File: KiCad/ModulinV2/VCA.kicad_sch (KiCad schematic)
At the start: 9 parts, among them IC9 AS3360D

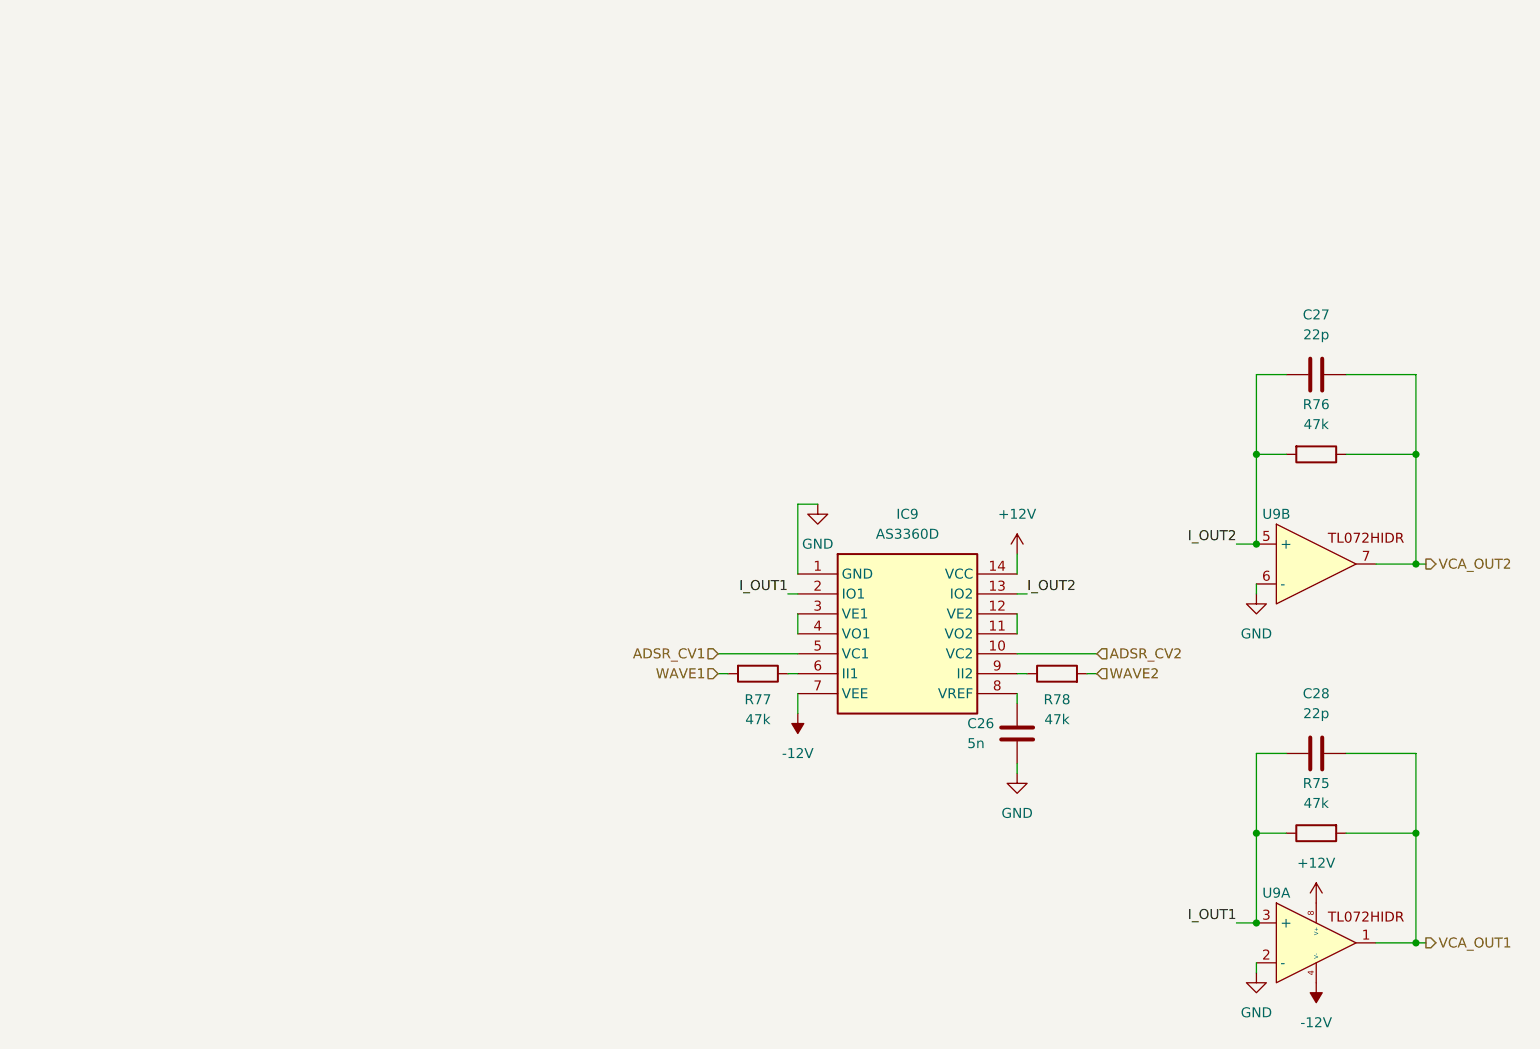
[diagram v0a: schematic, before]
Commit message: Modified Octave selector and started on waveform selection
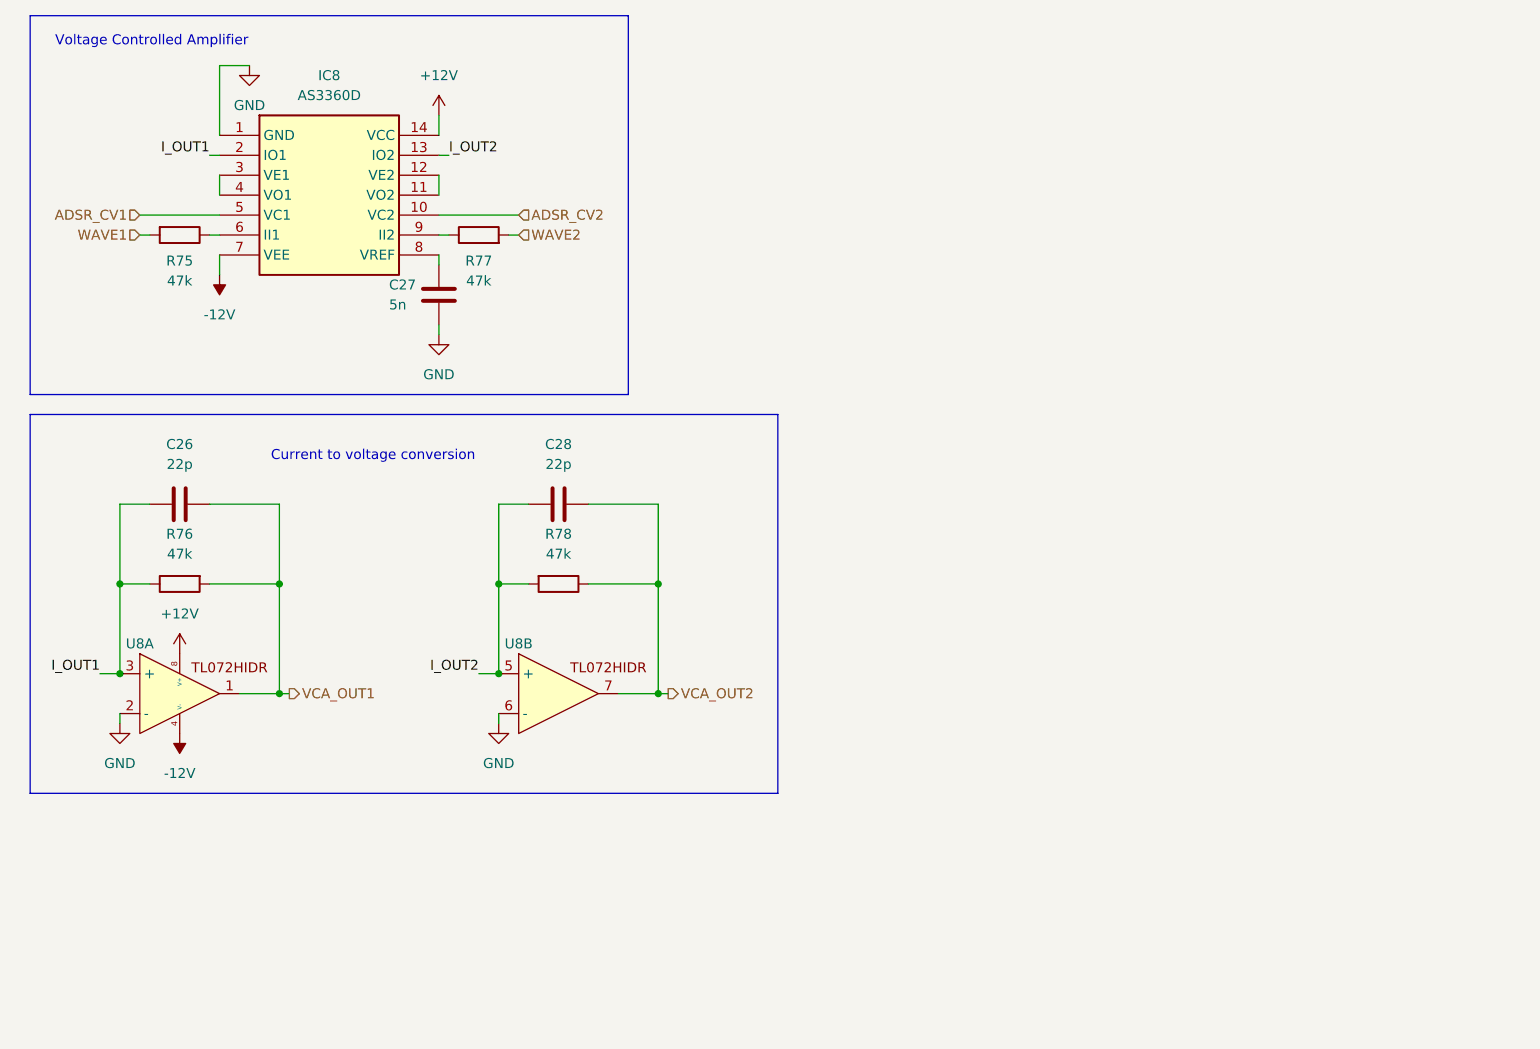
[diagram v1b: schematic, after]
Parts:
- renumbered C28 to C26, C26 to C27, C27 to C28, IC9 to IC8, R77 to R75, R75 to R76, R78 to R77, R76 to R78, U9 to U8
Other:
- note added: "Current to voltage conversion"
- note added: "Voltage Controlled Amplifier"
- moved on the sheet: C26, C27, C28, IC8, R75, R76, R77, R78, U8A, U8B

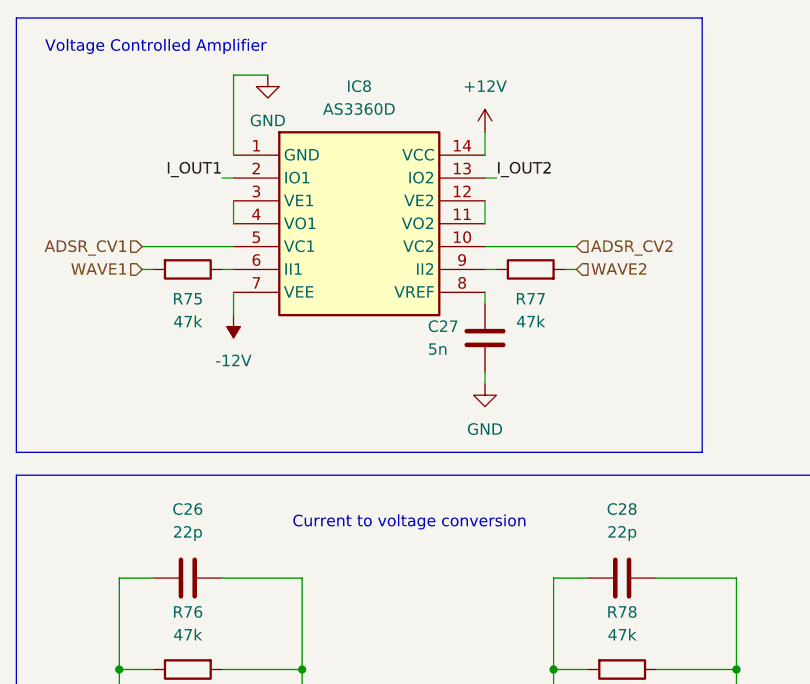
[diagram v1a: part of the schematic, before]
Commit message: Modified USB connection and added LEDs
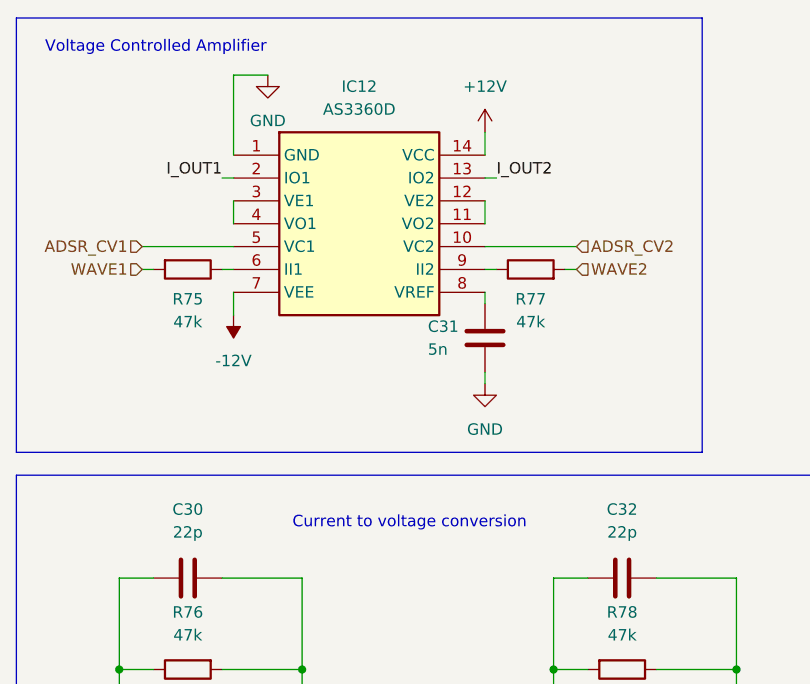
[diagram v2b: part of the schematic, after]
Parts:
- renumbered C26 to C30, C27 to C31, C28 to C32, IC8 to IC12
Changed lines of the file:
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@@
 		(dnp no)
 		(fields_autoplaced yes)
-		(property "Reference" "#PWR094"
+		(property "Reference" "#PWR0115"
 			(at 66.04 30.48 0)
 			(effects
@@
 			(project ""
 				(path "/c6b34a57-3941-4b56-8b80-1848c7f41082/a5a8abcc-50bb-4382-96d0-cbdb724bb6e9"
-					(reference "#PWR094")
+					(reference "#PWR0115")
 					(unit 1)
 				)
@@
 		(dnp no)
 		(fields_autoplaced yes)
-		(property "Reference" "#PWR090"
+		(property "Reference" "#PWR0111"
 			(at 33.02 99.06 0)
 			(effects
@@
 			(project "ModulinV2"
 				(path "/c6b34a57-3941-4b56-8b80-1848c7f41082/a5a8abcc-50bb-4382-96d0-cbdb724bb6e9"
-					(reference "#PWR090")
+					(reference "#PWR0111")
 					(unit 1)
 				)
@@
 		(dnp no)
 		(fields_autoplaced yes)
-		(property "Reference" "#PWR089"
+		(property "Reference" "#PWR0110"
 			(at 25.4 110.49 0)
 			(effects
@@
 			(project ""
 				(path "/c6b34a57-3941-4b56-8b80-1848c7f41082/a5a8abcc-50bb-4382-96d0-cbdb724bb6e9"
-					(reference "#PWR089")
+					(reference "#PWR0110")
 					(unit 1)
 				)
@@
 		(dnp no)
 		(fields_autoplaced yes)
-		(property "Reference" "#PWR095"
+		(property "Reference" "#PWR0116"
 			(at 66.04 60.96 0)
 			(effects
@@
 			(project ""
 				(path "/c6b34a57-3941-4b56-8b80-1848c7f41082/a5a8abcc-50bb-4382-96d0-cbdb724bb6e9"
-					(reference "#PWR095")
+					(reference "#PWR0116")
 					(unit 1)
 				)
@@
 		(dnp no)
 		(fields_autoplaced yes)
-		(property "Reference" "#PWR092"
+		(property "Reference" "#PWR0113"
 			(at 38.1 43.18 0)
 			(effects
@@
 			(project ""
 				(path "/c6b34a57-3941-4b56-8b80-1848c7f41082/a5a8abcc-50bb-4382-96d0-cbdb724bb6e9"
-					(reference "#PWR092")
+					(reference "#PWR0113")
 					(unit 1)
 				)
@@
 		(dnp no)
 		(fields_autoplaced yes)
-		(property "Reference" "#PWR093"
+		(property "Reference" "#PWR0114"
 			(at 41.91 26.67 0)
 			(effects
@@
 			(project ""
 				(path "/c6b34a57-3941-4b56-8b80-1848c7f41082/a5a8abcc-50bb-4382-96d0-cbdb724bb6e9"
-					(reference "#PWR093")
+					(reference "#PWR0114")
 					(unit 1)
 				)
@@
 		(dnp no)
 		(fields_autoplaced yes)
-		(property "Reference" "C26"
+		(property "Reference" "C30"
 			(at 33.02 68.58 90)
 			(effects
@@
 			(project ""
 				(path "/c6b34a57-3941-4b56-8b80-1848c7f41082/a5a8abcc-50bb-4382-96d0-cbdb724bb6e9"
-					(reference "C26")
+					(reference "C30")
 					(unit 1)
 				)
@@
 		(dnp no)
 		(fields_autoplaced yes)
-		(property "Reference" "#PWR091"
+		(property "Reference" "#PWR0112"
 			(at 33.02 101.6 0)
 			(effects
@@
 			(project "ModulinV2"
 				(path "/c6b34a57-3941-4b56-8b80-1848c7f41082/a5a8abcc-50bb-4382-96d0-cbdb724bb6e9"
-					(reference "#PWR091")
+					(reference "#PWR0112")
 					(unit 1)
 				)
@@
 		(dnp no)
 		(fields_autoplaced yes)
-		(property "Reference" "IC8"
+		(property "Reference" "IC12"
 			(at 52.07 21.59 0)
 			(effects
@@
 			(project ""
 				(path "/c6b34a57-3941-4b56-8b80-1848c7f41082/a5a8abcc-50bb-4382-96d0-cbdb724bb6e9"
-					(reference "IC8")
+					(reference "IC12")
 					(unit 1)
 				)
@@
 		(on_board yes)
 		(dnp no)
-		(property "Reference" "C27"
+		(property "Reference" "C31"
 			(at 59.69 48.26 0)
 			(effects
@@
 			(project ""
 				(path "/c6b34a57-3941-4b56-8b80-1848c7f41082/a5a8abcc-50bb-4382-96d0-cbdb724bb6e9"
-					(reference "C27")
+					(reference "C31")
 					(unit 1)
 				)
@@
 		(dnp no)
 		(fields_autoplaced yes)
-		(property "Reference" "#PWR096"
+		(property "Reference" "#PWR0117"
 			(at 73.66 110.49 0)
 			(effects
@@
 			(project ""
 				(path "/c6b34a57-3941-4b56-8b80-1848c7f41082/a5a8abcc-50bb-4382-96d0-cbdb724bb6e9"
-					(reference "#PWR096")
+					(reference "#PWR0117")
 					(unit 1)
 				)
@@
 		(dnp no)
 		(fields_autoplaced yes)
-		(property "Reference" "C28"
+		(property "Reference" "C32"
 			(at 81.28 68.58 90)
 			(effects
@@
 			(project ""
 				(path "/c6b34a57-3941-4b56-8b80-1848c7f41082/a5a8abcc-50bb-4382-96d0-cbdb724bb6e9"
-					(reference "C28")
-					(unit 1)
-				)
+					(reference "C32")
+					(unit 1)
+				)

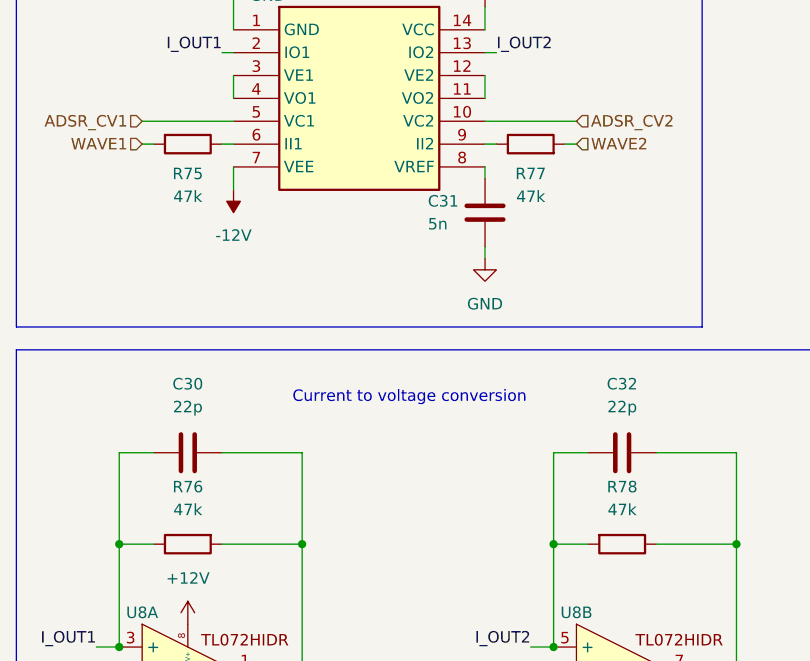
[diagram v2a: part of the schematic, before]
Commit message: Fleshed out the waveform select schematic a bit + general cleanup
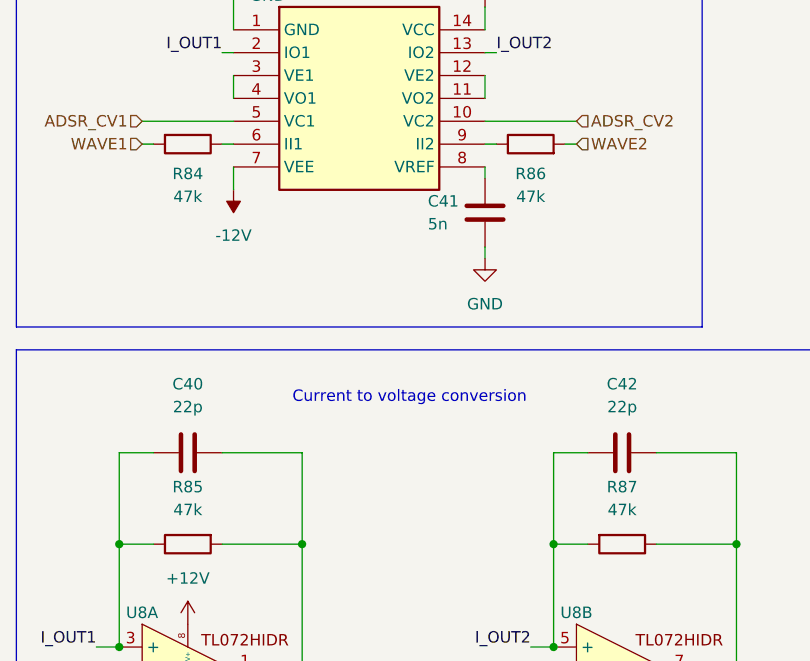
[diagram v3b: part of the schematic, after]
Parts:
- renumbered C30 to C40, C31 to C41, C32 to C42, R75 to R84, R76 to R85, R77 to R86, R78 to R87
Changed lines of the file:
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@@
 		(dnp no)
 		(fields_autoplaced yes)
-		(property "Reference" "R78"
+		(property "Reference" "R87"
 			(at 81.28 80.01 90)
 			(effects
@@
 			(project "ModulinV2"
 				(path "/c6b34a57-3941-4b56-8b80-1848c7f41082/a5a8abcc-50bb-4382-96d0-cbdb724bb6e9"
-					(reference "R78")
+					(reference "R87")
 					(unit 1)
 				)
@@
 		(dnp no)
 		(fields_autoplaced yes)
-		(property "Reference" "#PWR0115"
+		(property "Reference" "#PWR0143"
 			(at 66.04 30.48 0)
 			(effects
@@
 			(project ""
 				(path "/c6b34a57-3941-4b56-8b80-1848c7f41082/a5a8abcc-50bb-4382-96d0-cbdb724bb6e9"
-					(reference "#PWR0115")
+					(reference "#PWR0143")
 					(unit 1)
 				)
@@
 		(on_board yes)
 		(dnp no)
-		(property "Reference" "R77"
+		(property "Reference" "R86"
 			(at 71.12 45.212 90)
 			(effects
@@
 			(project "ModulinV2"
 				(path "/c6b34a57-3941-4b56-8b80-1848c7f41082/a5a8abcc-50bb-4382-96d0-cbdb724bb6e9"
-					(reference "R77")
+					(reference "R86")
 					(unit 1)
 				)
@@
 		(dnp no)
 		(fields_autoplaced yes)
-		(property "Reference" "#PWR0111"
+		(property "Reference" "#PWR0139"
 			(at 33.02 99.06 0)
 			(effects
@@
 			(project "ModulinV2"
 				(path "/c6b34a57-3941-4b56-8b80-1848c7f41082/a5a8abcc-50bb-4382-96d0-cbdb724bb6e9"
-					(reference "#PWR0111")
+					(reference "#PWR0139")
 					(unit 1)
 				)
@@
 		(on_board yes)
 		(dnp no)
-		(property "Reference" "R75"
+		(property "Reference" "R84"
 			(at 33.02 45.212 90)
 			(effects
@@
 			(project "ModulinV2"
 				(path "/c6b34a57-3941-4b56-8b80-1848c7f41082/a5a8abcc-50bb-4382-96d0-cbdb724bb6e9"
-					(reference "R75")
+					(reference "R84")
 					(unit 1)
 				)
@@
 		(dnp no)
 		(fields_autoplaced yes)
-		(property "Reference" "#PWR0110"
+		(property "Reference" "#PWR0138"
 			(at 25.4 110.49 0)
 			(effects
@@
 			(project ""
 				(path "/c6b34a57-3941-4b56-8b80-1848c7f41082/a5a8abcc-50bb-4382-96d0-cbdb724bb6e9"
-					(reference "#PWR0110")
+					(reference "#PWR0138")
 					(unit 1)
 				)
@@
 		(dnp no)
 		(fields_autoplaced yes)
-		(property "Reference" "#PWR0116"
+		(property "Reference" "#PWR0144"
 			(at 66.04 60.96 0)
 			(effects
@@
 			(project ""
 				(path "/c6b34a57-3941-4b56-8b80-1848c7f41082/a5a8abcc-50bb-4382-96d0-cbdb724bb6e9"
-					(reference "#PWR0116")
+					(reference "#PWR0144")
 					(unit 1)
 				)
@@
 		(dnp no)
 		(fields_autoplaced yes)
-		(property "Reference" "#PWR0113"
+		(property "Reference" "#PWR0141"
 			(at 38.1 43.18 0)
 			(effects
@@
 			(project ""
 				(path "/c6b34a57-3941-4b56-8b80-1848c7f41082/a5a8abcc-50bb-4382-96d0-cbdb724bb6e9"
-					(reference "#PWR0113")
+					(reference "#PWR0141")
 					(unit 1)
 				)
@@
 		(dnp no)
 		(fields_autoplaced yes)
-		(property "Reference" "#PWR0114"
+		(property "Reference" "#PWR0142"
 			(at 41.91 26.67 0)
 			(effects
@@
 			(project ""
 				(path "/c6b34a57-3941-4b56-8b80-1848c7f41082/a5a8abcc-50bb-4382-96d0-cbdb724bb6e9"
-					(reference "#PWR0114")
+					(reference "#PWR0142")
 					(unit 1)
 				)
@@
 		(dnp no)
 		(fields_autoplaced yes)
-		(property "Reference" "R76"
+		(property "Reference" "R85"
 			(at 33.02 80.01 90)
 			(effects
@@
 			(project ""
 				(path "/c6b34a57-3941-4b56-8b80-1848c7f41082/a5a8abcc-50bb-4382-96d0-cbdb724bb6e9"
-					(reference "R76")
+					(reference "R85")
 					(unit 1)
 				)
@@
 		(dnp no)
 		(fields_autoplaced yes)
-		(property "Reference" "C30"
+		(property "Reference" "C40"
 			(at 33.02 68.58 90)
 			(effects
@@
 			(project ""
 				(path "/c6b34a57-3941-4b56-8b80-1848c7f41082/a5a8abcc-50bb-4382-96d0-cbdb724bb6e9"
-					(reference "C30")
+					(reference "C40")
 					(unit 1)
 				)
@@
 		(dnp no)
 		(fields_autoplaced yes)
-		(property "Reference" "#PWR0112"
+		(property "Reference" "#PWR0140"
 			(at 33.02 101.6 0)
 			(effects
@@
 			(project "ModulinV2"
 				(path "/c6b34a57-3941-4b56-8b80-1848c7f41082/a5a8abcc-50bb-4382-96d0-cbdb724bb6e9"
-					(reference "#PWR0112")
+					(reference "#PWR0140")
 					(unit 1)
 				)
@@
 		(on_board yes)
 		(dnp no)
-		(property "Reference" "C31"
+		(property "Reference" "C41"
 			(at 59.69 48.26 0)
 			(effects
@@
 			(project ""
 				(path "/c6b34a57-3941-4b56-8b80-1848c7f41082/a5a8abcc-50bb-4382-96d0-cbdb724bb6e9"
-					(reference "C31")
+					(reference "C41")
 					(unit 1)
 				)
@@
 		(dnp no)
 		(fields_autoplaced yes)
-		(property "Reference" "#PWR0117"
+		(property "Reference" "#PWR0145"
 			(at 73.66 110.49 0)
 			(effects
@@
 			(project ""
 				(path "/c6b34a57-3941-4b56-8b80-1848c7f41082/a5a8abcc-50bb-4382-96d0-cbdb724bb6e9"
-					(reference "#PWR0117")
+					(reference "#PWR0145")
 					(unit 1)
 				)
@@
 		(dnp no)
 		(fields_autoplaced yes)
-		(property "Reference" "C32"
+		(property "Reference" "C42"
 			(at 81.28 68.58 90)
 			(effects
@@
 			(project ""
 				(path "/c6b34a57-3941-4b56-8b80-1848c7f41082/a5a8abcc-50bb-4382-96d0-cbdb724bb6e9"
-					(reference "C32")
-					(unit 1)
-				)
+					(reference "C42")
+					(unit 1)
+				)
